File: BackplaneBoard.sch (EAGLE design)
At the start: 4 parts

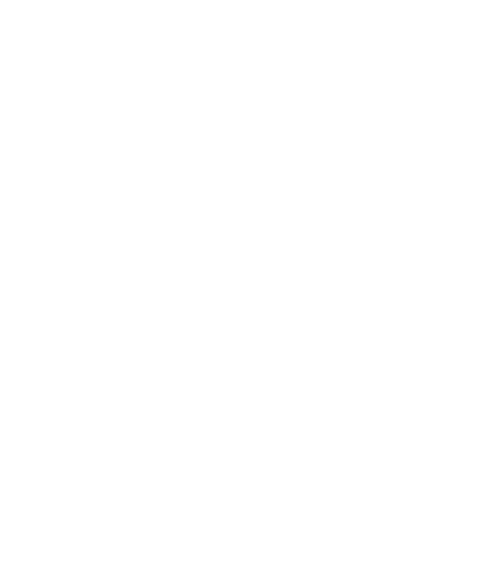
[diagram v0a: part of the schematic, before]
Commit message: added holes for standoffs
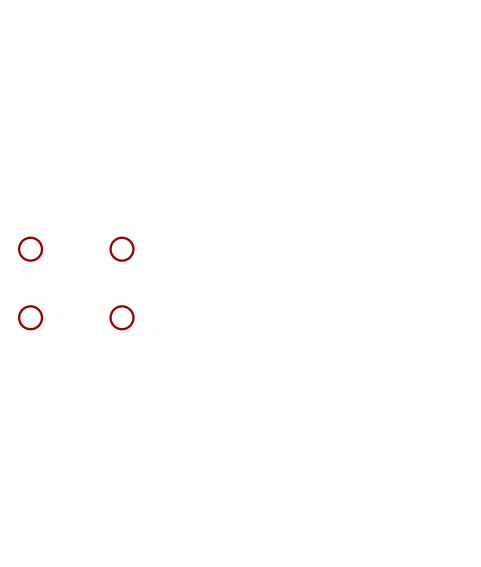
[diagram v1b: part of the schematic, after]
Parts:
- added H1, H2, H3, H4: STAND-OFF, SparkFun-Hardware:STAND-OFF
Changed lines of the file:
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@@
 <layer number="112" name="tSilk" color="7" fill="1" visible="yes" active="yes"/>
 <layer number="113" name="IDFDebug" color="7" fill="1" visible="yes" active="yes"/>
+<layer number="114" name="Badge_Outline" color="7" fill="1" visible="yes" active="yes"/>
 <layer number="116" name="Patch_BOT" color="9" fill="4" visible="yes" active="yes"/>
 <layer number="118" name="Rect_Pads" color="7" fill="1" visible="yes" active="yes"/>
@@
 <part name="U$3" library="ESC_to_Backplane_Connectors" deviceset="ESC2BACKPLANE" device=""/>
 <part name="U$4" library="ESC_to_Backplane_Connectors" deviceset="ESC2BACKPLANE" device=""/>
+<part name="H1" library="SparkFun-Hardware" library_urn="urn:adsk.eagle:library:519" deviceset="STAND-OFF" device="" package3d_urn="urn:adsk.eagle:package:38630/1"/>
+<part name="H2" library="SparkFun-Hardware" library_urn="urn:adsk.eagle:library:519" deviceset="STAND-OFF" device="" package3d_urn="urn:adsk.eagle:package:38630/1"/>
+<part name="H3" library="SparkFun-Hardware" library_urn="urn:adsk.eagle:library:519" deviceset="STAND-OFF" device="" package3d_urn="urn:adsk.eagle:package:38630/1"/>
+<part name="H4" library="SparkFun-Hardware" library_urn="urn:adsk.eagle:library:519" deviceset="STAND-OFF" device="" package3d_urn="urn:adsk.eagle:package:38630/1"/>
 </parts>
 <sheets>
@@
 <instance part="U$4" gate="G$1" x="317.5" y="45.72"/>
 <instance part="U$4" gate="G$2" x="370.84" y="48.26"/>
+<instance part="H1" gate="G$1" x="17.78" y="60.96"/>
+<instance part="H2" gate="G$1" x="27.94" y="60.96"/>
+<instance part="H3" gate="G$1" x="17.78" y="53.34"/>
+<instance part="H4" gate="G$1" x="27.94" y="53.34"/>
 </instances>
 <busses>
@@
 will not be understood (or retained) with this version.
 </note>
+<note version="8.3" severity="warning">
+Since Version 8.3, EAGLE supports the association of 3D packages
+with devices in libraries, schematics, and board files. Those 3D
+packages will not be understood (or retained) with this version.
+</note>
 </compatibility>

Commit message: consistent
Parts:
- added U$14, U$15, U$16, U$17, U$18, U$19, U$20, U$21, U$22, U$5: PHCONNECTOR, PHConnector:PHCONNECTOR
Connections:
- new net +12V: U$17.P$1, U$17.P$2, U$17.P$3, U$17.P$4, U$1G$2.17, U$1G$2.18, U$1G$2.19, U$1G$2.20, U$1G$2.21, U$1G$2.22, U$1G$2.23, U$1G$2.24, U$1G$2.25, U$1G$2.26, U$1G$2.27, U$1G$2.28, U$1G$2.29, U$1G$2.30, U$1G$2.31, U$1G$2.32, U$20.P$1, U$20.P$2, U$20.P$3, U$20.P$4, U$2G$1.P$10, U$2G$1.P$11, U$2G$1.P$12, U$2G$1.P$13, U$2G$1.P$23, U$2G$1.P$24, U$2G$1.P$25, U$2G$1.P$26, U$2G$1.P$27, U$2G$1.P$9, U$2G$2.P$A, U$2G$2.P$B, U$2G$2.P$C, U$2G$2.P$D, U$2G$2.P$E, U$2G$2.P$O, U$2G$2.P$P, U$2G$2.P$Q, U$2G$2.P$R, U$2G$2.P$S, U$3G$1.P$10, U$3G$1.P$11, U$3G$1.P$12, U$3G$1.P$13, U$3G$1.P$23, U$3G$1.P$24, U$3G$1.P$25, U$3G$1.P$26, U$3G$1.P$27, U$3G$1.P$9, U$3G$2.P$A, U$3G$2.P$B, U$3G$2.P$C, U$3G$2.P$D, U$3G$2.P$E, U$3G$2.P$O, U$3G$2.P$P, U$3G$2.P$Q, U$3G$2.P$R, U$3G$2.P$S, U$4G$1.P$10, U$4G$1.P$11, U$4G$1.P$12, U$4G$1.P$13, U$4G$1.P$23, U$4G$1.P$24, U$4G$1.P$25, U$4G$1.P$26, U$4G$1.P$27, U$4G$1.P$9, U$4G$2.P$A, U$4G$2.P$B, U$4G$2.P$C, U$4G$2.P$D, U$4G$2.P$E, U$4G$2.P$O, U$4G$2.P$P, U$4G$2.P$Q, U$4G$2.P$R, U$4G$2.P$S
- new net +3V3: U$1G$1.1, U$1G$1.10, U$1G$1.11, U$1G$1.12, U$1G$1.17, U$1G$1.18, U$1G$1.19, U$1G$1.2, U$1G$1.3, U$1G$1.4, U$1G$1.9, U$2G$2.P$G, U$2G$2.P$H, U$2G$2.P$U, U$2G$2.P$V, U$3G$2.P$G, U$3G$2.P$H, U$3G$2.P$U, U$3G$2.P$V, U$4G$2.P$G, U$4G$2.P$H, U$4G$2.P$U, U$4G$2.P$V
- new net +5V: U$14.P$1, U$14.P$2, U$14.P$3, U$14.P$4, U$1G$1.13, U$1G$1.14, U$1G$1.15, U$1G$1.16, U$1G$1.22, U$1G$1.23, U$1G$1.24, U$1G$1.5, U$1G$1.6, U$1G$1.7, U$1G$1.8, U$21.P$1, U$21.P$2, U$21.P$3, U$21.P$4
- new net CAN_H: U$16.P$2, U$19.P$2, U$1G$1.20, U$2G$1.P$6, U$3G$1.P$6, U$4G$1.P$6
- new net CAN_L: U$16.P$3, U$19.P$3, U$1G$1.21, U$2G$1.P$7, U$3G$1.P$7, U$4G$1.P$7
- new net GND: U$15.P$1, U$15.P$2, U$15.P$3, U$15.P$4, U$18.P$1, U$18.P$2, U$18.P$3, U$18.P$4, U$1G$2.1, U$1G$2.10, U$1G$2.11, U$1G$2.12, U$1G$2.13, U$1G$2.14, U$1G$2.15, U$1G$2.16, U$1G$2.2, U$1G$2.3, U$1G$2.4, U$1G$2.5, U$1G$2.6, U$1G$2.7, U$1G$2.8, U$1G$2.9, U$22.P$1, U$22.P$2, U$22.P$3, U$22.P$4, U$2G$1.P$1, U$2G$1.P$15, U$2G$1.P$16, U$2G$1.P$17, U$2G$1.P$18, U$2G$1.P$2, U$2G$1.P$3, U$2G$1.P$4, U$2G$2.P$AA, U$2G$2.P$BB, U$2G$2.P$J, U$2G$2.P$K, U$2G$2.P$L, U$2G$2.P$M, U$2G$2.P$N, U$2G$2.P$X, U$2G$2.P$Y, U$2G$2.P$Z, U$3G$1.P$1, U$3G$1.P$15, U$3G$1.P$16, U$3G$1.P$17, U$3G$1.P$18, U$3G$1.P$2, U$3G$1.P$3, U$3G$1.P$4, U$3G$2.P$AA, U$3G$2.P$BB, U$3G$2.P$J, U$3G$2.P$K, U$3G$2.P$L, U$3G$2.P$M, U$3G$2.P$N, U$3G$2.P$X, U$3G$2.P$Y, U$3G$2.P$Z, U$4G$1.P$1, U$4G$1.P$15, U$4G$1.P$16, U$4G$1.P$17, U$4G$1.P$18, U$4G$1.P$2, U$4G$1.P$3, U$4G$1.P$4, U$4G$2.P$AA, U$4G$2.P$BB, U$4G$2.P$J, U$4G$2.P$K, U$4G$2.P$L, U$4G$2.P$M, U$4G$2.P$N, U$4G$2.P$X, U$4G$2.P$Y, U$4G$2.P$Z
- new net PROG_1: U$5.P$2
- new net PROG_2: U$5.P$3
- new net PROG_3: U$5.P$4
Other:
- note added: "+5V Fan"
- note added: "12V to Logic"
- note added: "12V to Solenoid"
- note added: "5V to Logic"
- note added: "CAN to Logic"
- note added: "CAN to Solenoid"
- note added: "GND Fan"
- note added: "GND to Logic"
- note added: "GND to Solenoid"
- note added: "Programmer"

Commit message: workable revised state. need new connectors and programming muxing routing
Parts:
- removed U$17, U$21: PHCONNECTOR, PHConnector:PHCONNECTOR
- added C1, C2: 0.1uF, SparkFun-Capacitors:0.1UF-0603-25V-(+80/-20%)
- added U1, U2: SN74CBTLV3257PWR, SN74CBTLV3257PWR:SN74CBTLV3257PWR
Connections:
- new net NRST_1: U$2G$1.P$20, U1.3B2
- new net NRST_2: U$3G$1.P$20, U2.3B2
- new net NRST_3: U$4G$1.P$20, U2.3B1
- new net NRST_IN: U$22.P$2, U1.3A
- new net NRST_MUX2: U1.3B1, U2.3A
- new net SWCLK_1: U$2G$1.P$22, U1.2B2
- new net SWCLK_2: U$3G$1.P$22, U2.2B2
- new net SWCLK_3: U$4G$1.P$22, U2.2B1
- new net SWCLK_IN: U$22.P$4, U1.2A
- new net SWCLK_MUX2: U1.2B1, U2.2A
- new net SWDIO_1: U$2G$1.P$21, U1.1B2
- new net SWDIO_2: U$3G$1.P$21, U2.1B2
- new net SWDIO_3: U$4G$1.P$21, U2.1B1
- new net SWDIO_IN: U$22.P$3, U1.1A
- new net SWDIO_MUX2: U1.1B1, U2.1A
- net +12V: now also U$14.P$3, U$14.P$4, U$16.P$4; no longer U$17.P$1, U$17.P$2, U$17.P$3, U$17.P$4, U$20.P$1, U$20.P$2, U$20.P$3, U$20.P$4
- net +3V3: now also C1.1, C2.1, U$22.P$1, U1.VCC, U2.VCC
- net +5V: now also U$19.P$4, U$20.P$3, U$20.P$4; no longer U$14.P$3, U$14.P$4, U$21.P$1, U$21.P$2, U$21.P$3, U$21.P$4
- net CAN_H: now also U$18.P$2
- net CAN_L: now also U$18.P$3
- net GND: now also C1.2, C2.2, U$16.P$1, U$19.P$1, U$20.P$1, U$20.P$2, U$5.P$1, U1.GND, U1.OE, U2.GND, U2.OE; no longer U$18.P$2, U$18.P$3, U$22.P$1, U$22.P$2, U$22.P$3, U$22.P$4
- net PROG_1: now also U$2G$1.P$5, U1.S
- net PROG_2: now also U$3G$1.P$5, U2.S
- net PROG_3: now also U$4G$1.P$5
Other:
- note added: "CAN DEBUG CANH CANL GND"
- note added: "LOGIC: 3 x 5V 3 x GND CANH CANL"
- note added: "PROGRAM PROG x 3 GND 3V3? NRST? SWDIO? SWCLK?"
- note added: "SOLENOIDs: 12V GND CANH CANL"
- note removed: "12V to Logic"
- note removed: "12V to Solenoid"
- note removed: "5V to Logic"
- note removed: "GND to Logic"
- note removed: "GND to Solenoid"

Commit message: finished backplane mux
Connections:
- removed net NRST_1: U$2G$1.P$20, U1.3B2
- removed net NRST_2: U$3G$1.P$20, U2.3B2
- removed net NRST_3: U$4G$1.P$20, U2.3B1
- removed net NRST_IN: U$22.P$2, U1.3A
- removed net NRST_MUX2: U1.3B1, U2.3A
- new net NRST: U$22.P$2, U$2G$1.P$20, U$3G$1.P$20, U$4G$1.P$20
- net PROG_2: no longer U2.S
- net PROG_3: now also U2.S
- net SWCLK_2: now also U2.2B1; no longer U2.2B2
- net SWCLK_3: now also U2.2B2; no longer U2.2B1
- net SWDIO_2: now also U2.1B1; no longer U2.1B2
- net SWDIO_3: now also U2.1B2; no longer U2.1B1
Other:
- note added: "PROG_1 high chooses esc 1 to program PROG_1 low and PROG_3 high chooses esc 3 PROG_1 low and PROG_3 low chooses esc 2"
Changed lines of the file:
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@@
 <part name="P+6" library="supply1" library_urn="urn:adsk.eagle:library:371" deviceset="+12V" device=""/>
 <part name="P+10" library="supply1" library_urn="urn:adsk.eagle:library:371" deviceset="+12V" device=""/>
-<part name="GND13" library="audio amplifier example" library_urn="urn:adsk.eagle:library:970892" deviceset="GND" device="" value="SUP"/>
 <part name="GND14" library="audio amplifier example" library_urn="urn:adsk.eagle:library:970892" deviceset="GND" device="" value="SUP"/>
 <part name="P+13" library="supply1" library_urn="urn:adsk.eagle:library:371" deviceset="+12V" device=""/>
@@
 SWCLK?
 </text>
+<text x="78.74" y="248.92" size="1.778" layer="91">PROG_1 high chooses esc 1 to program
+PROG_1 low and PROG_3 high chooses esc 3
+PROG_1 low and PROG_3 low chooses esc 2</text>
 </plain>
 <instances>
@@
 <instance part="P+6" gate="1" x="378.46" y="261.62"/>
 <instance part="P+10" gate="1" x="325.12" y="35.56"/>
-<instance part="GND13" gate="G$1" x="116.84" y="137.16"/>
 <instance part="GND14" gate="G$1" x="149.86" y="137.16"/>
 <instance part="P+13" gate="1" x="154.94" y="134.62"/>
@@
 <pinref part="U$1" gate="G$2" pin="12"/>
 <wire x1="121.92" y1="137.16" x2="116.84" y2="137.16" width="0.1524" layer="91"/>
-<pinref part="GND13" gate="G$1" pin="GND"/>
 <junction x="116.84" y="137.16"/>
 <pinref part="GND15" gate="G$1" pin="GND"/>
@@
 </segment>
 <segment>
+<pinref part="U$3" gate="G$1" pin="P$5"/>
+<wire x1="330.2" y1="279.4" x2="320.04" y2="279.4" width="0.1524" layer="91"/>
+<label x="320.04" y="279.4" size="1.778" layer="95"/>
+</segment>
+</net>
+<net name="PROG_3" class="0">
+<segment>
+<pinref part="U$5" gate="G$1" pin="P$4"/>
+<wire x1="27.94" y1="83.82" x2="15.24" y2="83.82" width="0.1524" layer="91"/>
+<label x="15.24" y="83.82" size="1.778" layer="95"/>
+</segment>
+<segment>
+<pinref part="U$4" gate="G$1" pin="P$5"/>
+<wire x1="279.4" y1="53.34" x2="271.78" y2="53.34" width="0.1524" layer="91"/>
+<label x="271.78" y="53.34" size="1.778" layer="95"/>
+</segment>
+<segment>
 <pinref part="U2" gate="G$1" pin="S"/>
 <wire x1="152.4" y1="231.14" x2="137.16" y2="231.14" width="0.1524" layer="91"/>
 <label x="137.16" y="231.14" size="1.778" layer="95"/>
 </segment>
-<segment>
-<pinref part="U$3" gate="G$1" pin="P$5"/>
-<wire x1="330.2" y1="279.4" x2="320.04" y2="279.4" width="0.1524" layer="91"/>
-<label x="320.04" y="279.4" size="1.778" layer="95"/>
-</segment>
-</net>
-<net name="PROG_3" class="0">
-<segment>
-<pinref part="U$5" gate="G$1" pin="P$4"/>
-<wire x1="27.94" y1="83.82" x2="15.24" y2="83.82" width="0.1524" layer="91"/>
-<label x="15.24" y="83.82" size="1.778" layer="95"/>
-</segment>
-<segment>
-<pinref part="U$4" gate="G$1" pin="P$5"/>
-<wire x1="279.4" y1="53.34" x2="271.78" y2="53.34" width="0.1524" layer="91"/>
-<label x="271.78" y="53.34" size="1.778" layer="95"/>
-</segment>
 </net>
 <net name="SWDIO_IN" class="0">
@@
 </segment>
 </net>
-<net name="NRST_IN" class="0">
-<segment>
-<pinref part="U1" gate="G$1" pin="3A"/>
-<wire x1="177.8" y1="241.3" x2="187.96" y2="241.3" width="0.1524" layer="91"/>
-<label x="180.34" y="241.3" size="1.778" layer="95"/>
-</segment>
+<net name="NRST" class="0">
 <segment>
 <pinref part="U$22" gate="G$1" pin="P$2"/>
@@
 <label x="30.48" y="73.66" size="1.778" layer="95"/>
 </segment>
+<segment>
+<pinref part="U$2" gate="G$1" pin="P$20"/>
+<wire x1="312.42" y1="127" x2="325.12" y2="127" width="0.1524" layer="91"/>
+<label x="317.5" y="127" size="1.778" layer="95"/>
+</segment>
+<segment>
+<pinref part="U$4" gate="G$1" pin="P$20"/>
+<wire x1="312.42" y1="48.26" x2="325.12" y2="48.26" width="0.1524" layer="91"/>
+<label x="317.5" y="48.26" size="1.778" layer="95"/>
+</segment>
+<segment>
+<pinref part="U$3" gate="G$1" pin="P$20"/>
+<wire x1="363.22" y1="274.32" x2="378.46" y2="274.32" width="0.1524" layer="91"/>
+<label x="368.3" y="274.32" size="1.778" layer="95"/>
+</segment>
 </net>
 <net name="SWDIO_1" class="0">
@@
 </segment>
 </net>
-<net name="NRST_1" class="0">
-<segment>
-<pinref part="U1" gate="G$1" pin="3B2"/>
-<wire x1="177.8" y1="243.84" x2="187.96" y2="243.84" width="0.1524" layer="91"/>
-<label x="180.34" y="243.84" size="1.778" layer="95"/>
-</segment>
-<segment>
-<pinref part="U$2" gate="G$1" pin="P$20"/>
-<wire x1="312.42" y1="127" x2="325.12" y2="127" width="0.1524" layer="91"/>
-<label x="317.5" y="127" size="1.778" layer="95"/>
-</segment>
-</net>
-<net name="NRST_MUX2" class="0">
-<segment>
-<pinref part="U1" gate="G$1" pin="3B1"/>
-<wire x1="177.8" y1="246.38" x2="187.96" y2="246.38" width="0.1524" layer="91"/>
-<label x="180.34" y="246.38" size="1.778" layer="95"/>
-</segment>
-<segment>
-<pinref part="U2" gate="G$1" pin="3A"/>
-<wire x1="177.8" y1="213.36" x2="193.04" y2="213.36" width="0.1524" layer="91"/>
-<label x="185.42" y="213.36" size="1.778" layer="95"/>
-</segment>
-</net>
 <net name="SWCLK_1" class="0">
 <segment>
@@
 <net name="SWCLK_2" class="0">
 <segment>
+<pinref part="U$3" gate="G$1" pin="P$22"/>
+<wire x1="363.22" y1="264.16" x2="378.46" y2="264.16" width="0.1524" layer="91"/>
+<label x="368.3" y="264.16" size="1.778" layer="95"/>
+</segment>
+<segment>
+<pinref part="U2" gate="G$1" pin="2B1"/>
+<wire x1="152.4" y1="220.98" x2="137.16" y2="220.98" width="0.1524" layer="91"/>
+<label x="137.16" y="220.98" size="1.778" layer="95"/>
+</segment>
+</net>
+<net name="SWCLK_3" class="0">
+<segment>
+<pinref part="U$4" gate="G$1" pin="P$22"/>
+<wire x1="312.42" y1="38.1" x2="325.12" y2="38.1" width="0.1524" layer="91"/>
+<label x="317.5" y="38.1" size="1.778" layer="95"/>
+</segment>
+<segment>
 <pinref part="U2" gate="G$1" pin="2B2"/>
 <wire x1="152.4" y1="218.44" x2="137.16" y2="218.44" width="0.1524" layer="91"/>
 <label x="137.16" y="218.44" size="1.778" layer="95"/>
 </segment>
-<segment>
-<pinref part="U$3" gate="G$1" pin="P$22"/>
-<wire x1="363.22" y1="264.16" x2="378.46" y2="264.16" width="0.1524" layer="91"/>
-<label x="368.3" y="264.16" size="1.778" layer="95"/>
-</segment>
-</net>
-<net name="SWCLK_3" class="0">
-<segment>
-<pinref part="U2" gate="G$1" pin="2B1"/>
-<wire x1="152.4" y1="220.98" x2="137.16" y2="220.98" width="0.1524" layer="91"/>
-<label x="137.16" y="220.98" size="1.778" layer="95"/>
-</segment>
-<segment>
-<pinref part="U$4" gate="G$1" pin="P$22"/>
-<wire x1="312.42" y1="38.1" x2="325.12" y2="38.1" width="0.1524" layer="91"/>
-<label x="317.5" y="38.1" size="1.778" layer="95"/>
-</segment>
 </net>
 <net name="SWDIO_2" class="0">
+<segment>
+<pinref part="U$3" gate="G$1" pin="P$21"/>
+<wire x1="363.22" y1="269.24" x2="378.46" y2="269.24" width="0.1524" layer="91"/>
+<label x="368.3" y="269.24" size="1.778" layer="95"/>
+</segment>
+<segment>
+<pinref part="U2" gate="G$1" pin="1B1"/>
+<wire x1="152.4" y1="228.6" x2="137.16" y2="228.6" width="0.1524" layer="91"/>
+<label x="137.16" y="228.6" size="1.778" layer="95"/>
+</segment>
+</net>
+<net name="SWDIO_3" class="0">
+<segment>
+<pinref part="U$4" gate="G$1" pin="P$21"/>
+<wire x1="312.42" y1="43.18" x2="325.12" y2="43.18" width="0.1524" layer="91"/>
+<label x="317.5" y="43.18" size="1.778" layer="95"/>
+</segment>
 <segment>
 <pinref part="U2" gate="G$1" pin="1B2"/>
@@
 <label x="137.16" y="226.06" size="1.778" layer="95"/>
 </segment>
-<segment>
-<pinref part="U$3" gate="G$1" pin="P$21"/>
-<wire x1="363.22" y1="269.24" x2="378.46" y2="269.24" width="0.1524" layer="91"/>
-<label x="368.3" y="269.24" size="1.778" layer="95"/>
-</segment>
-</net>
-<net name="SWDIO_3" class="0">
-<segment>
-<pinref part="U2" gate="G$1" pin="1B1"/>
-<wire x1="152.4" y1="228.6" x2="137.16" y2="228.6" width="0.1524" layer="91"/>
-<label x="137.16" y="228.6" size="1.778" layer="95"/>
-</segment>
-<segment>
-<pinref part="U$4" gate="G$1" pin="P$21"/>
-<wire x1="312.42" y1="43.18" x2="325.12" y2="43.18" width="0.1524" layer="91"/>
-<label x="317.5" y="43.18" size="1.778" layer="95"/>
-</segment>
-</net>
-<net name="NRST_2" class="0">
-<segment>
-<pinref part="U2" gate="G$1" pin="3B2"/>
-<wire x1="177.8" y1="215.9" x2="193.04" y2="215.9" width="0.1524" layer="91"/>
-<label x="185.42" y="215.9" size="1.778" layer="95"/>
-</segment>
-<segment>
-<pinref part="U$3" gate="G$1" pin="P$20"/>
-<wire x1="363.22" y1="274.32" x2="378.46" y2="274.32" width="0.1524" layer="91"/>
-<label x="368.3" y="274.32" size="1.778" layer="95"/>
-</segment>
-</net>
-<net name="NRST_3" class="0">
-<segment>
-<pinref part="U2" gate="G$1" pin="3B1"/>
-<wire x1="177.8" y1="218.44" x2="193.04" y2="218.44" width="0.1524" layer="91"/>
-<label x="185.42" y="218.44" size="1.778" layer="95"/>
-</segment>
-<segment>
-<pinref part="U$4" gate="G$1" pin="P$20"/>
-<wire x1="312.42" y1="48.26" x2="325.12" y2="48.26" width="0.1524" layer="91"/>
-<label x="317.5" y="48.26" size="1.778" layer="95"/>
-</segment>
-</net>
+</net>

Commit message: few minor improvements to the mux
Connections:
- net GND: now also U1.3A, U1.4A, U2.3A, U2.4A
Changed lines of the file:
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@@
 <instance part="+3V10" gate="G$1" x="180.34" y="264.16"/>
 <instance part="+3V11" gate="G$1" x="180.34" y="236.22"/>
-<instance part="GND21" gate="G$1" x="182.88" y="228.6"/>
-<instance part="GND22" gate="G$1" x="182.88" y="256.54"/>
+<instance part="GND21" gate="G$1" x="182.88" y="213.36"/>
+<instance part="GND22" gate="G$1" x="182.88" y="241.3"/>
 <instance part="C2" gate="G$1" x="203.2" y="254.508" smashed="yes">
 <attribute name="NAME" x="204.724" y="257.429" size="1.778" layer="95" font="vector"/>
@@
 <pinref part="U2" gate="G$1" pin="OE"/>
 <wire x1="177.8" y1="228.6" x2="182.88" y2="228.6" width="0.1524" layer="91"/>
+<wire x1="182.88" y1="228.6" x2="182.88" y2="220.98" width="0.1524" layer="91"/>
 <pinref part="GND21" gate="G$1" pin="GND"/>
+<pinref part="U2" gate="G$1" pin="4A"/>
+<wire x1="182.88" y1="220.98" x2="182.88" y2="213.36" width="0.1524" layer="91"/>
+<wire x1="177.8" y1="220.98" x2="182.88" y2="220.98" width="0.1524" layer="91"/>
+<junction x="182.88" y="220.98"/>
+<pinref part="U2" gate="G$1" pin="3A"/>
+<wire x1="177.8" y1="213.36" x2="182.88" y2="213.36" width="0.1524" layer="91"/>
+<junction x="182.88" y="213.36"/>
 </segment>
 <segment>
 <pinref part="U1" gate="G$1" pin="OE"/>
 <wire x1="177.8" y1="256.54" x2="182.88" y2="256.54" width="0.1524" layer="91"/>
+<wire x1="182.88" y1="256.54" x2="182.88" y2="248.92" width="0.1524" layer="91"/>
 <pinref part="GND22" gate="G$1" pin="GND"/>
-</segment>
-<segment>
+<pinref part="U1" gate="G$1" pin="4A"/>
+<wire x1="182.88" y1="248.92" x2="182.88" y2="241.3" width="0.1524" layer="91"/>
+<wire x1="177.8" y1="248.92" x2="182.88" y2="248.92" width="0.1524" layer="91"/>
+<junction x="182.88" y="248.92"/>
+<pinref part="U1" gate="G$1" pin="3A"/>
+<wire x1="177.8" y1="241.3" x2="182.88" y2="241.3" width="0.1524" layer="91"/>
+<junction x="182.88" y="241.3"/>
+</segment>
+<segment>
